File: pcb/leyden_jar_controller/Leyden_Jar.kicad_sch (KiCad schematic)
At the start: 92 parts, among them J1 USB_C_Receptacle_USB2.0, J2 Switch matrix connector, J3 SWD/I2C, J4 Ext Conn, SW1 B3U-1000P, SW2 B3U-1000P, SW3 B3U-1000P, SW4 B3U-1000P, U1 W25Q16JVUXIQ, U10 MCP4716A0T-E/CH, U2 LMV339, U3 USBLC6-2SC6, U4 ADP122AUJZ-3.3-R7, U5 RP2040, U6 LMV339, U8 PCA9557PW,118, Y1 12MHz

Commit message: [feature] Leyden Jar schematic converted to Kicad 10.
Co-Authored-By: Claude Opus 5.5 <noreply@anthropic.com>
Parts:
- U4: value ADP122AUJZ-3.3-R7 -> ADP122AUJZ-3.3-R7

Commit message: [feature] V2 schematic: RP2350B, new power path and new connectors.
RP2350B replaces the RP2040; PCA9557, column resistors, polyfuse and
top-side buttons are removed. Adds the AP22653 USB power switch,
TLV74311 1.1 V core LDO, TPS7A2033 3.3 V LDO, 8 MB flash, ABM8 crystal,
2x4 Ext Port with USB D+/D-, Qwiic, SWD, split, display, encoder and
expansion headers. New project symbols: AP22653W6, TLV743xxPDBV,
MCP4716xxx-xCH.

Co-Authored-By: Claude Opus 5.5 <noreply@anthropic.com>
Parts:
- removed F1: mSMD110-16V, Fuse:Fuse_1210_3225Metric, symbol Device:Fuse
- removed J3: SWD/I2C, Leyden_Jar:PinHeader_2x03_P2.54mm_Horizontal, symbol Connector_Generic:Conn_02x03_Odd_Even
- removed J4: Ext Conn, Leyden_Jar:PinHeader_2x03_P2.54mm_Horizontal, symbol Connector_Generic:Conn_02x03_Odd_Even
- removed R14, R15, R16, R18, R20, R21, R22, R23, R24, R26, R28, R29, R30, R31, R32, R34, R47, R48, R49: 1000, Resistor_SMD:R_0402_1005Metric, symbol Device:R_Small
- removed SW3, SW4: B3U-1000P, Leyden_Jar:SPST_B3U-1000P, symbol Switch:SW_Push
- removed U5: RP2040, QFN-56-RP2040, symbol Leyden_Jar:RP2040
- removed U8: PCA9557PW,118, Leyden_Jar:TSSOP-16_4.4x5mm_P0.65mm, symbol Interface_Expansion:PCA9557PW
- added C22, C24, C25: 1u, Capacitor_SMD:C_0402_1005Metric, symbol Device:C_Small
- added C23, C26, C27, C28, C29, C31, C32: 100n, Capacitor_SMD:C_0402_1005Metric, symbol Device:C_Small
- added C30: 4.7u, Capacitor_SMD:C_0805_2012Metric, symbol Device:C_Small
- added J10: Expansion, Connector_PinHeader_2.54mm:PinHeader_1x06_P2.54mm_Vertical, symbol Connector_Generic:Conn_01x06
- added J4: Ext Port, Leyden_Jar:PinHeader_2x04_P2.54mm_Horizontal, symbol Connector_Generic:Conn_02x04_Odd_Even
- added J5: Qwiic, Connector_JST:JST_SH_SM04B-SRSS-TB_1x04-1MP_P1.00mm_Horizontal, symbol Connector_Generic:Conn_01x04
- added J6: SWD, Connector_JST:JST_SH_SM03B-SRSS-TB_1x03-1MP_P1.00mm_Horizontal, symbol Connector_Generic:Conn_01x03
- added J7: Split, Connector_PinHeader_2.54mm:PinHeader_1x03_P2.54mm_Vertical, symbol Connector_Generic:Conn_01x03
- added J8: Display, Connector_PinHeader_2.54mm:PinHeader_1x08_P2.54mm_Vertical, symbol Connector_Generic:Conn_01x08
- added J9: Encoder, Connector_PinHeader_2.54mm:PinHeader_1x05_P2.54mm_Vertical, symbol Connector_Generic:Conn_01x05
- added JP1: TFT VCC, Jumper:SolderJumper-3_P1.3mm_Bridged12_RoundedPad1.0x1.5mm, symbol Jumper:SolderJumper_3_Bridged12
- added R51: 20k, Resistor_SMD:R_0402_1005Metric, symbol Device:R_Small
- added R52: 33, Resistor_SMD:R_0402_1005Metric, symbol Device:R_Small
- added R53, R54: 10k, Resistor_SMD:R_0402_1005Metric, symbol Device:R_Small
- added U5: RP2350B, Package_DFN_QFN:QFN-80-1EP_10x10mm_P0.4mm_EP3.4x3.4mm, symbol MCU_RaspberryPi:RP2350B
- added U7: TLV74311PDBVR, Package_TO_SOT_SMD:SOT-23-5, symbol Leyden_Jar:TLV743xxPDBV
- added U8: AP22653W6-7, Package_TO_SOT_SMD:SOT-23-6, symbol Leyden_Jar:AP22653W6
- added U9: USBLC6-2SC6, Leyden_Jar:SOT-23-6, symbol Power_Protection:USBLC6-2SC6
- C14, C15: value 30p -> 15p; LCSC C1570 -> C1548
- C16: value 4.7u -> 10u; LCSC C1779 -> C15850
- C2: value 1u -> 4.7u; footprint Capacitor_SMD:C_0402_1005Metric -> Capacitor_SMD:C_0805_2012Metric; LCSC C52923 -> C1779
- U1: value W25Q16JVUXIQ -> W25Q64JVXGIM; footprint Leyden_Jar:USON8_3x2mm -> Package_SON:WSON-8-1EP_4x4mm_P0.8mm_EP2.2x3mm; LCSC C2843335 -> C6604688; Mouser 454-W25Q16JVUXIQTR -> (none)
- U10: symbol Analog_DAC:MCP4725xxx-xCH -> Leyden_Jar:MCP4716xxx-xCH
- U4: value ADP122AUJZ-3.3-R7 -> TPS7A2033PDBVR; footprint Leyden_Jar:TSOT-23-5 -> Package_TO_SOT_SMD:SOT-23-5; symbol Regulator_Linear:ADP7142AUJZ-3.3 -> Regulator_Linear:TPS7A20xxxDBV; LCSC C143910 -> C2862740; Mouser 584-ADP122AUJZ-3.3R7 -> (none)
- Y1: value 12MHz -> ABM8-272-T3; LCSC C9002 -> C20625731
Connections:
- net +5V: now also C23.1, C24.1, J4.3 (Pin_3), J7.1 (Pin_1), JP1.3 (B), U7.1 (IN), U7.3 (EN), U8.6 (OUT), U9.5 (VBUS)
- net 1V1: now also C25.1, C29.1, U5.10 (DVDD), U5.32 (DVDD), U5.51 (DVDD), U7.5 (OUT)
- net 3V3: now also R10.1, R11.1, U10.6 (VREF), C26.1, C27.1, C28.1, J10.1 (Pin_1), J4.7 (Pin_7), J5.2 (Pin_2), J9.4 (Pin_4), JP1.1 (A), R52.1, R53.1, R54.1, U5.15 (IOVDD), U5.24 (IOVDD), U5.29 (IOVDD), U5.41 (IOVDD), U5.5 (IOVDD), U5.50 (IOVDD), U5.59 (ADC_AVDD), U5.60 (IOVDD), U5.64 (VREG_VIN), U5.68 (USB_OTP_VDD), U5.69 (QSPI_IOVDD), U5.76 (IOVDD); no longer R10.2, R11.2
- net COL0: now also J2.13 (Pin_13), U5.6 (GPIO8)
- net COL1: now also J2.14 (Pin_14), U5.7 (GPIO9)
- net COL10: now also J2.23 (Pin_23), U5.20 (GPIO20)
- net COL11: now also J2.24 (Pin_24), U5.21 (GPIO21)
- net COL12: now also J2.25 (Pin_25), U5.22 (GPIO22)
- net COL13: now also J2.26 (Pin_26), U5.23 (GPIO23)
- net COL14: now also J2.27 (Pin_27), U5.25 (GPIO24)
- net COL15: now also J2.28 (Pin_28), U5.26 (GPIO25)
- net COL16: now also J2.29 (Pin_29), U5.36 (GPIO28)
- net COL17: now also J2.30 (Pin_30), U5.37 (GPIO29)
- net COL2: now also J2.15 (Pin_15), U5.8 (GPIO10)
- net COL3: now also J2.16 (Pin_16), U5.9 (GPIO11)
- net COL4: now also J2.17 (Pin_17), U5.11 (GPIO12)
- net COL5: now also J2.18 (Pin_18), U5.12 (GPIO13)
- net COL6: now also J2.19 (Pin_19), U5.13 (GPIO14)
- net COL7: now also J2.20 (Pin_20), U5.14 (GPIO15)
- net COL8: now also J2.21 (Pin_21), U5.18 (GPIO18)
- net COL9: now also J2.22 (Pin_22), U5.19 (GPIO19)
- net F_D+: now also J4.2 (Pin_2)
- net F_D-: now also J4.1 (Pin_1)
- net GND: now also C22.2, C23.2, C24.2, C25.2, C26.2, C27.2, C28.2, C29.2, C30.2, C31.2, C32.2, J10.6 (Pin_6), J4.8 (Pin_8), J5.1 (Pin_1), J6.2 (Pin_2), J7.2 (Pin_2), J8.1 (Pin_1), J9.5 (Pin_5), R51.2, U5.62 (VREG_PGND), U5.65 (VREG_FB), U5.81 (GND), U7.2 (GND), U8.2 (GND), U9.2 (GND)
- net LED0: now also U5.53 (GPIO42/ADC2)
- net LED1: now also U5.54 (GPIO43/ADC3)
- net LED2: now also U5.55 (GPIO44/ADC4)
- net PS2_ENABLE: now also J4.5 (Pin_5), U5.49 (GPIO40/ADC0)
- net QSPI_SD0: now also U5.72 (QSPI_SD0)
- net QSPI_SD1: now also U5.74 (QSPI_SD1)
- net QSPI_SD2: now also U5.73 (QSPI_SD2)
- net QSPI_SD3: now also U5.70 (QSPI_SD3)
- net QSPI_SS: now also U5.75 (~{QSPI_SS})
- net ROW0: now also U5.77 (GPIO0)
- net ROW1: now also U5.78 (GPIO1)
- net ROW2: now also U5.79 (GPIO2)
- net ROW3: now also U5.80 (GPIO3)
- net ROW4: now also U5.1 (GPIO4)
- net ROW5: now also U5.2 (GPIO5)
- net ROW6: now also U5.3 (GPIO6)
- net ROW7: now also U5.4 (GPIO7)
- net RUN: now also U5.35 (RUN)
- net SCL: now also R10.2, J5.4 (Pin_4), U5.17 (GPIO17); no longer R10.1
- net SDA: now also R11.2, J5.3 (Pin_3), U5.16 (GPIO16); no longer R11.1
- net SOLENOID_ENABLE: now also J4.4 (Pin_4), U5.27 (GPIO26)
- net SOLENOID_PULSE: now also J4.6 (Pin_6), U5.28 (GPIO27)
- net SWCLK: now also J6.1 (Pin_1), U5.33 (SWCLK)
- net USB_D+: now also U5.67 (USB_DP)
- net USB_D-: now also U5.66 (USB_DM)
- net VBUS: now also C22.1, U8.1 (IN), U8.3 (EN)
- net XIN: now also U5.30 (XIN)
- net XOUT: now also U5.31 (XOUT)
- net ~{QSPI_SCLK} renamed QSPI_SCLK
- net QSPI_SCLK: now also U5.71 (QSPI_SCLK)
- new net: R51.1, U8.5 (ILIM)
- new net ENCODER_A: C31.1, J9.1 (Pin_1), R53.2, U5.46 (GPIO37)
- new net ENCODER_B: C32.1, J9.2 (Pin_2), R54.2, U5.47 (GPIO38)
- new net ENCODER_BUTTON: J9.3 (Pin_3), U5.48 (GPIO39)
- new net EXP_GP32: J10.2 (Pin_2), U5.40 (GPIO32)
- new net EXP_GP41: J10.3 (Pin_3), U5.52 (GPIO41/ADC1)
- new net EXP_GP46: J10.4 (Pin_4), U5.57 (GPIO46/ADC6)
- new net EXP_GP47: J10.5 (Pin_5), U5.58 (GPIO47/ADC7)
- new net SWDIO: J6.3 (Pin_3), U5.34 (SWDIO)
- new net TFT_BLK: J8.8 (Pin_8), U5.45 (GPIO36)
- new net TFT_CS: J8.7 (Pin_7), U5.42 (GPIO33)
- new net TFT_DC: J8.6 (Pin_6), U5.43 (GPIO34)
- new net TFT_MOSI: J8.4 (Pin_4), U5.39 (GPIO31)
- new net TFT_RST: J8.5 (Pin_5), U5.44 (GPIO35)
- new net TFT_SCK: J8.3 (Pin_3), U5.38 (GPIO30)
- new net TFT_VCC: J8.2 (Pin_2), JP1.2 (C)
- new net UART_DATA: J7.3 (Pin_3), U5.56 (GPIO45/ADC5), U9.1 (I/O1), U9.6 (I/O1)
- new net VREG_AVDD: C30.1, R52.2, U5.61 (VREG_AVDD)
- no-connect marks 8 -> 7
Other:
- note added: "1.1 V core supply (fed from +5V)"
- note added: "1V1 bulk"
- note added: "3.3 V voltage regulator"
- note added: "Expansion header"
- note added: "Extra RP2350B decoupling"
- note added: "PS2 daughterboard presence pull-down"
- note added: "Rotary encoder (RC debounce on A/B)"
- note added: "SWD and Qwiic connectors"
- note added: "Split connector"
- note added: "TFT display (ST7789 module), VCC by solder jumper"
- note added: "USB power switch (current limit, replaces the polyfuse)"
- note added: "USB_OTP_VDD"
- note added: "VREG_AVDD RC filter"
- note added: "VREG_VIN"
- note removed: "IO expander for solenoid and leds"
- note removed: "SWD/I2C connector"
- note removed: "USB_VDD"
- note removed: "VREG_IN"
- note removed: "VREG_OUT"
- note removed: "Voltage regulator and over-current protection"
- moved on the sheet: R10, R11

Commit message: [cleanup] V2 schematic: bypass capacitors grouped per RP2350B supply pin.
Decoupling caps are grouped by supply pin (VREG_VIN + VREG_AVDD, 1V1 bulk,
DVDD, IOVDD, QSPI_IOVDD, USB_OTP_VDD, ADC_AVDD) in the MCU bypass block.
The 33R + 4.7uF VREG_AVDD filter is removed: with the internal regulator
disabled, VREG_AVDD joins VREG_VIN on 3V3 per RP2350 datasheet Figure 24.

Co-Authored-By: Claude Opus 5.5 <noreply@anthropic.com>
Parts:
- removed C30: 4.7u, Capacitor_SMD:C_0805_2012Metric, symbol Device:C_Small
- removed R52: 33, Resistor_SMD:R_0402_1005Metric, symbol Device:R_Small
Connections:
- net VREG_AVDD is gone; now on net 3V3: U5.61 (VREG_AVDD)
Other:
- note added: "QSPI_IOVDD"
- note added: "VREG_VIN + VREG_AVDD"
- note removed: "Extra RP2350B decoupling"
- note removed: "VREG_AVDD RC filter"
- note removed: "VREG_VIN"
- moved on the sheet: C10, C11, C12, C13, C26, C27, C28, C29, C3, C4, C5, C6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

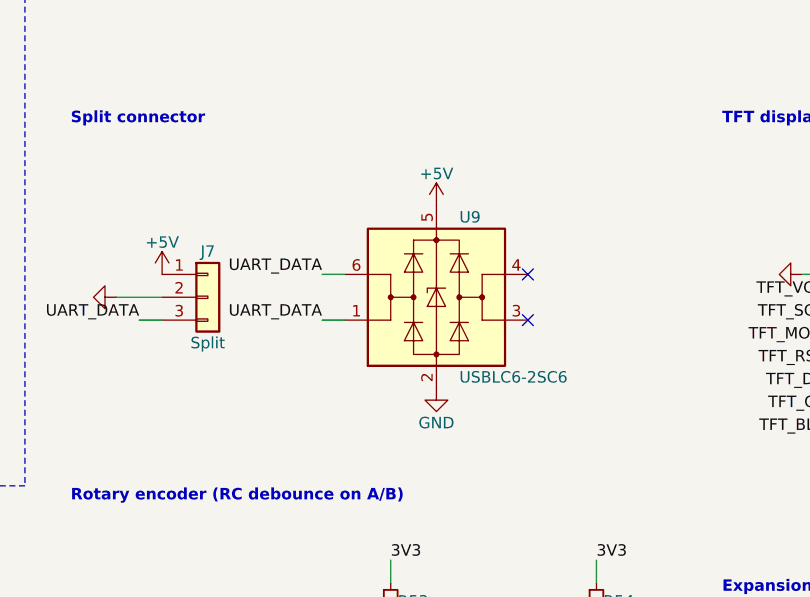
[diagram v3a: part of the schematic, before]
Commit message: [cleanup] V2 schematic: single TVS on the split data line.
The USBLC6-2SC6 on the split header is replaced by one ESD9B3.3ST5G TVS
on UART_DATA. The split 5V stays on +5V after the AP22653, whose bulk
capacitance absorbs ESD on that pin.

Co-Authored-By: Claude Opus 5.5 <noreply@anthropic.com>
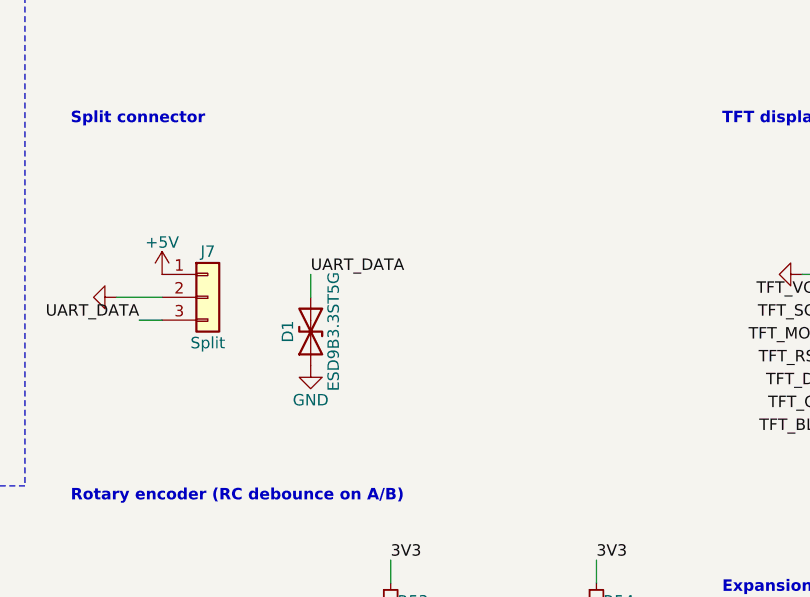
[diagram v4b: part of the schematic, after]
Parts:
- removed U9: USBLC6-2SC6, Leyden_Jar:SOT-23-6, symbol Power_Protection:USBLC6-2SC6
- added D1: ESD9B3.3ST5G, Diode_SMD:D_SOD-923, symbol Device:D_TVS
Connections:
- net GND: now also D1.1 (A1)
- net UART_DATA: now also D1.2 (A2)
- no-connect marks 7 -> 5

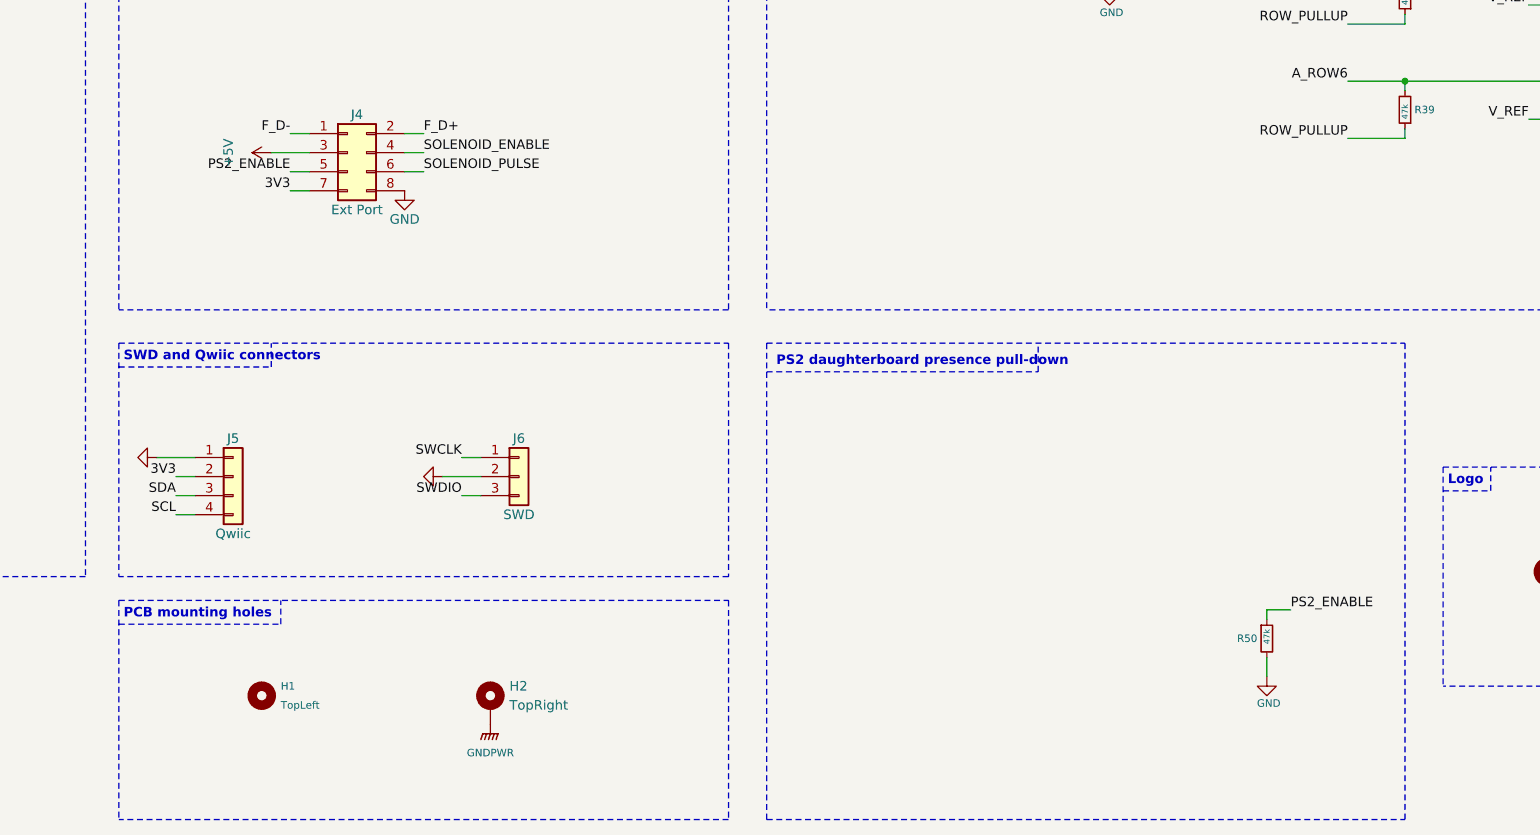
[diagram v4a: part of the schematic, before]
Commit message: [cleanup] V2 schematic: PS2_ENABLE pull-down R50 moved next to J4.
Co-Authored-By: Claude Opus 5.5 <noreply@anthropic.com>
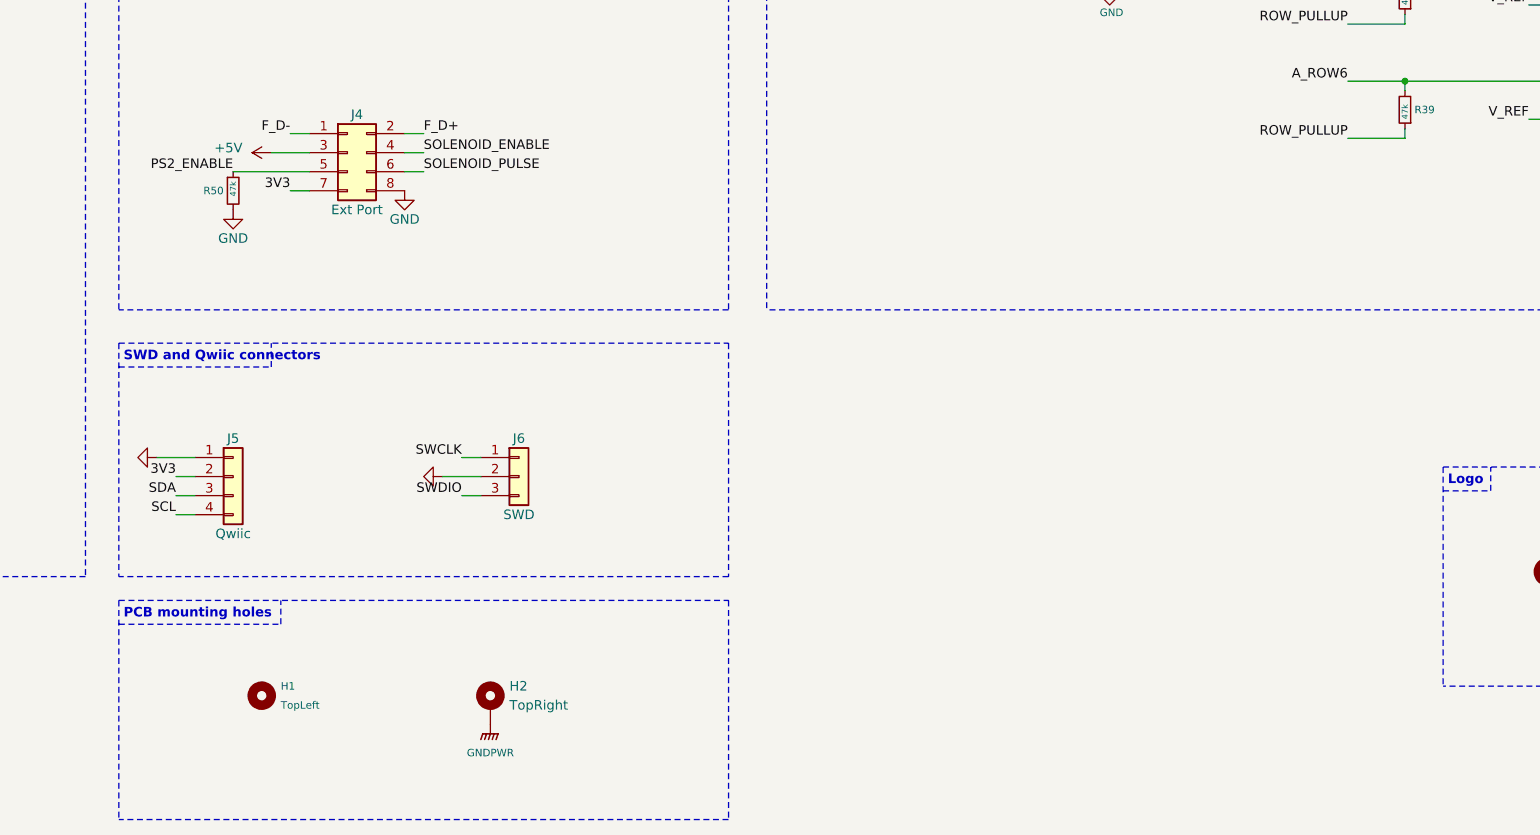
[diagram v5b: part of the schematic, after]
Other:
- note removed: "PS2 daughterboard presence pull-down"
- moved on the sheet: R50

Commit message: [feature] V2: single-row J7 breakout header and Rev 3 SWD/I2C header J3 back.
Connector placement feedback:
- J10 (expansion), J7 (split) and J8 (TFT display) merged into one 1x17 header J7 so a ribbon cable can be
  soldered in one row. Pins 1-6 expansion + GND, 7-9 split (+5V, GND, UART_DATA), 10-17 ST7789 module order.
  On the board: y 1.4, pin 1 x 12.761 to pin 17 x 53.401, centered between H1's pad and the USB-C body.
- JST SH J5 (Qwiic) and J6 (SWD) reverted to Rev 3's 2x3 SWD/I2C header J3 (same pinout and footprint), placed
  at Rev 3's x but lower to clear J7 (origin 11.55, 5.08).

Co-Authored-By: Claude Opus 5.5 <noreply@anthropic.com>
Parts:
- removed J5: Qwiic, Connector_JST:JST_SH_SM04B-SRSS-TB_1x04-1MP_P1.00mm_Horizontal, symbol Connector_Generic:Conn_01x04
- removed J6: SWD, Connector_JST:JST_SH_SM03B-SRSS-TB_1x03-1MP_P1.00mm_Horizontal, symbol Connector_Generic:Conn_01x03
- removed J7: Split, Connector_PinHeader_2.54mm:PinHeader_1x03_P2.54mm_Vertical, symbol Connector_Generic:Conn_01x03
- removed J8: Display, Connector_PinHeader_2.54mm:PinHeader_1x08_P2.54mm_Vertical, symbol Connector_Generic:Conn_01x08
- added J3: SWD/I2C, Leyden_Jar:PinHeader_2x03_P2.54mm_Horizontal, symbol Connector_Generic:Conn_02x03_Odd_Even
- J7: renamed from J10; value Expansion -> Breakout; footprint Connector_PinHeader_2.54mm:PinHeader_1x06_P2.54mm_Vertical -> Connector_PinHeader_2.54mm:PinHeader_1x17_P2.54mm_Vertical; symbol Connector_Generic:Conn_01x06 -> Connector_Generic:Conn_01x17
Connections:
- net +5V: now also J7.7 (Pin_7)
- net 3V3: now also J3.2 (Pin_2)
- net GND: now also J7.10 (Pin_10), J7.8 (Pin_8), J3.1 (Pin_1)
- net SCL: now also J3.6 (Pin_6)
- net SDA: now also J3.4 (Pin_4)
- net SWCLK: now also J3.3 (Pin_3)
- net SWDIO: now also J3.5 (Pin_5)
- net TFT_BLK: now also J7.17 (Pin_17)
- net TFT_CS: now also J7.16 (Pin_16)
- net TFT_DC: now also J7.15 (Pin_15)
- net TFT_MOSI: now also J7.13 (Pin_13)
- net TFT_RST: now also J7.14 (Pin_14)
- net TFT_SCK: now also J7.12 (Pin_12)
- net TFT_VCC: now also J7.11 (Pin_11)
- net UART_DATA: now also J7.9 (Pin_9)
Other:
- note added: "Breakout header (expansion, split link, ST7789 TFT), TFT VCC by solder jumper"
- note added: "SWD/I2C header (Rev 3)"
- note added: "Split link ESD (J7 pin 9)"
- note removed: "Expansion header"
- note removed: "SWD and Qwiic connectors"
- note removed: "Split connector"
- note removed: "TFT display (ST7789 module), VCC by solder jumper"

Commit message: [feature] V2: top-side RUN/BOOT buttons back, J3 and J9 aligned.
Connector placement feedback:
- SW3/SW4 (top side, B3U-1000P) re-added in parallel with SW1 (RUN) and SW2 (USB_BOOT), as in Rev 3.
  All four buttons vertical, left of the USB-C below the J7 row, top and bottom pairs at the same XY:
  RUN (51.70, 5.6), BOOT (55.00, 5.6), pitch 3.3 mm (was 3.7).
- J3 moved so its pin 1 sits under J7 pin 1 (x 12.761).
- J9 moved so its pin 5 sits above J2 pin 1 (x 1.60); the comparator block (U2, U6 and their resistors and
  capacitors) moved 0.2 mm right with it to keep the same clearances.

Co-Authored-By: Claude Opus 5.5 <noreply@anthropic.com>
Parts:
- added SW3, SW4: B3U-1000P, Leyden_Jar:SPST_B3U-1000P, symbol Switch:SW_Push
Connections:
- net GND: now also SW3.2, SW4.2
- net RUN: now also SW3.1
- net USB_BOOT: now also SW4.1
